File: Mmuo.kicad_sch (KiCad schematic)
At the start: 93 parts, among them IC1 A121-001-T&R, IC2 BQ24253RGER, IC3 ADPL40502AUJZ-1.8-R7, J1 USB_C_Receptacle_USB2.0_16P, J2 B2B-PH-K-S, J3 SW_Debug, Q1 BSS84, Q2 BSS138, Q3 MMBT3904, SW1 PTS815, U1 USBLC6-2SC6, U2 RT9166A-33GXL, U3 EKMB1309113K, U4 STM32WB55CGU6, U5 MCP9808_MSOP, Y1 24MHz, Y2 32MHz, Y3 32K768

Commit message: Schematics Verifcation
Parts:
- added D8: LED, LED_SMD:LED_0805_2012Metric_Pad1.15x1.40mm_HandSolder, symbol Device:LED
- added R24: 220, Resistor_SMD:R_0603_1608Metric_Pad0.98x0.95mm_HandSolder, symbol Device:R
- D1, D2, D3, D6, D7: footprint LED_SMD:LED_1206_3216Metric_Pad1.42x1.75mm_HandSolder -> LED_SMD:LED_0805_2012Metric_Pad1.15x1.40mm_HandSolder
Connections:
- net GND: now also D8.1 (K)
- net Pair_Mode: now reaches U4.29 (PB1)
- net Pair_Mode: now also R24.1
- net RF_LP renamed RF_LPF
- new net: D8.2 (A), R24.2
- no-connect marks 19 -> 18
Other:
- note added: "WHITE"
- note added: "YELLOW"
- note removed: "HSMD-C150"
- note removed: "HSMG-C150"
- moved on the sheet: AE1, AE2, C19, C20, C21, C22, C23, C24, C25, C26, C27, C29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

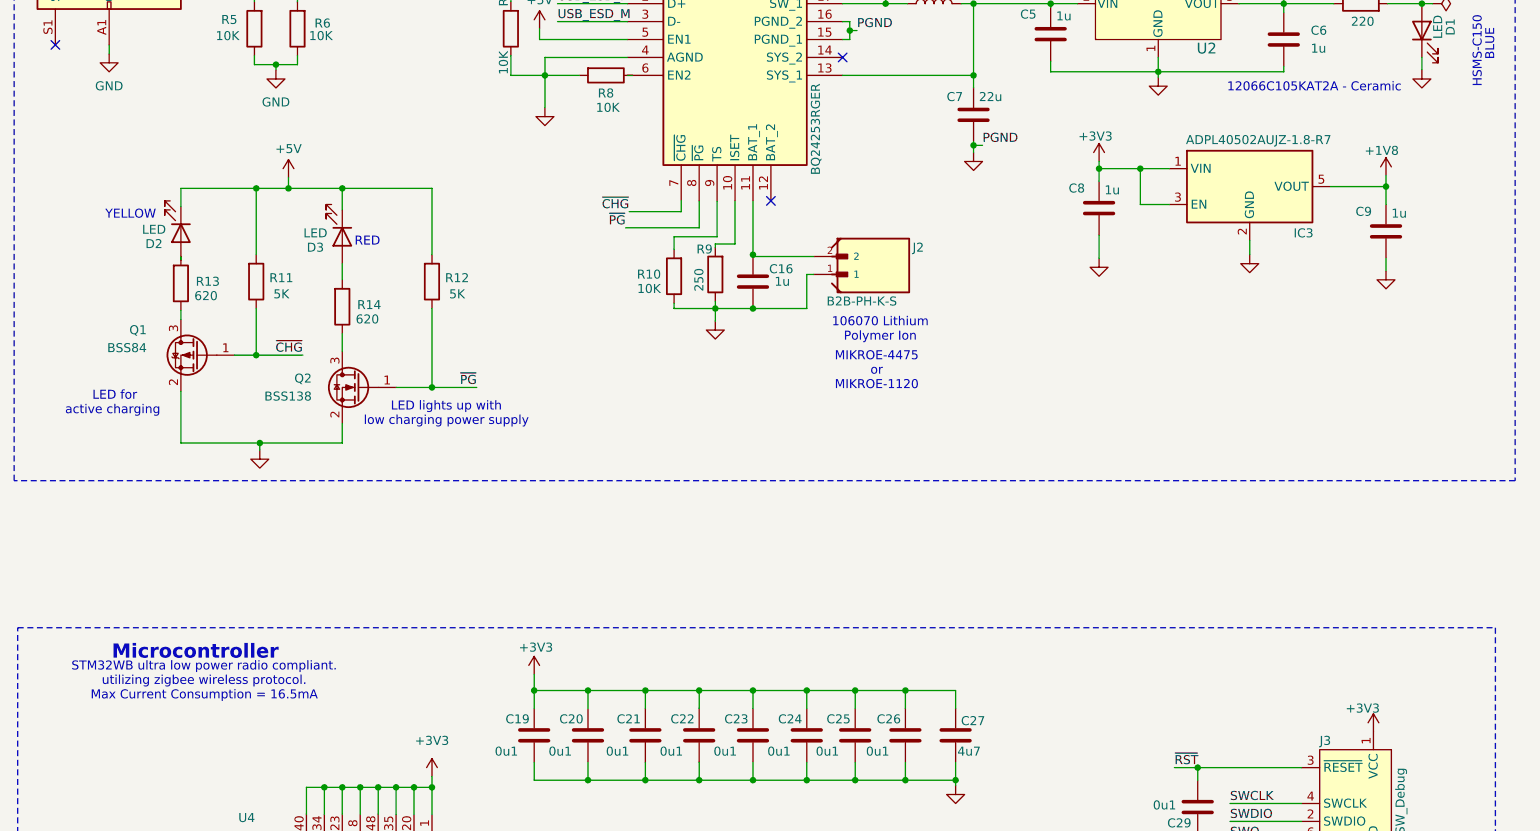
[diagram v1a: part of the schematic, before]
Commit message: replacing 3v3 LDO to boost-buck converter
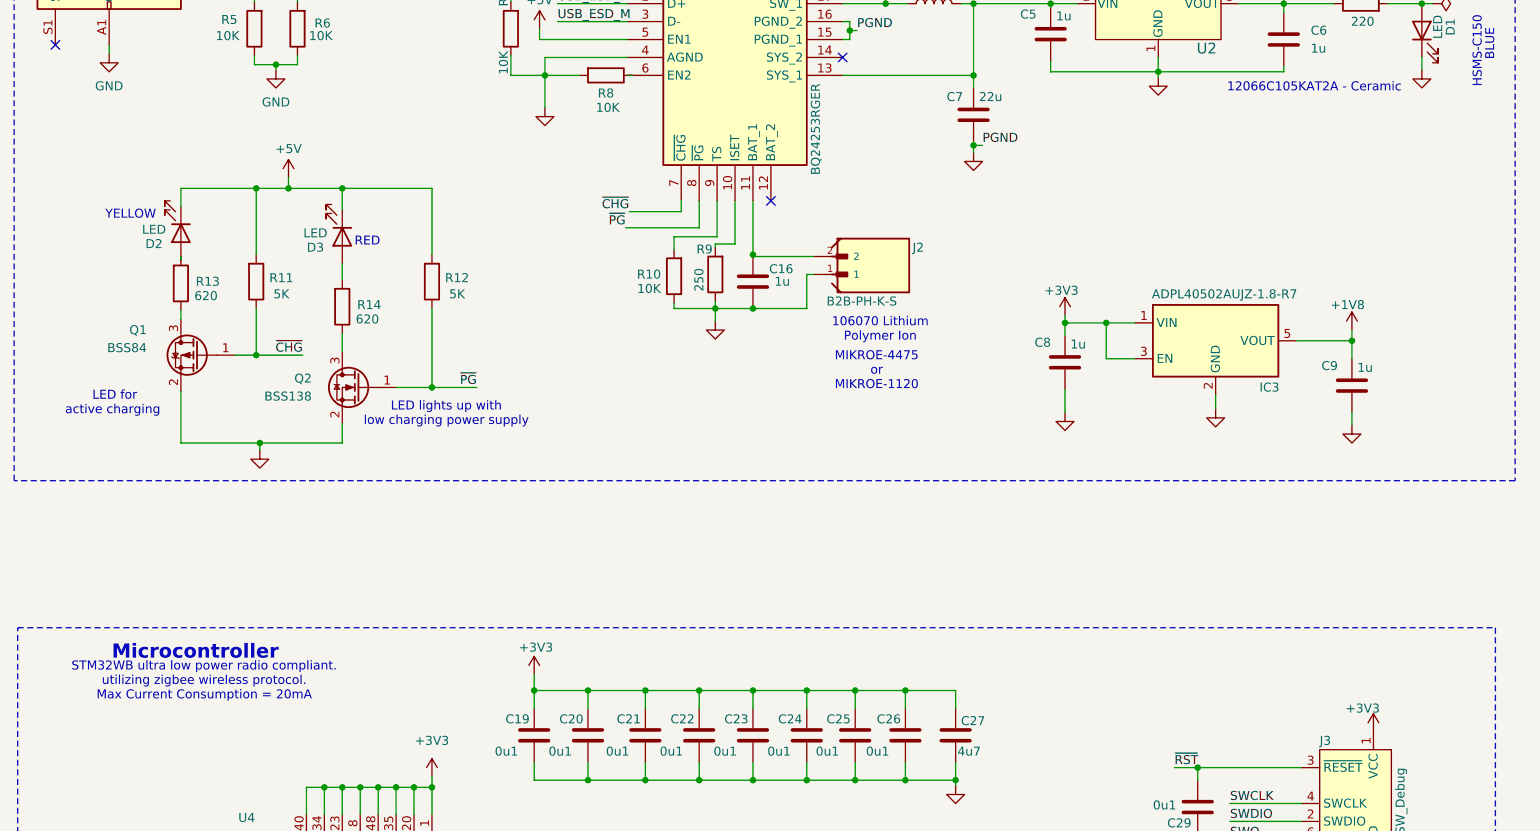
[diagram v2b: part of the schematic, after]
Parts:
- L1: footprint Inductor_SMD:L_0805_2012Metric_Pad1.15x1.40mm_HandSolder -> Inductor_SMD:L_0805_2012Metric_Pad1.05x1.20mm_HandSolder
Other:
- note added: "STM32WB ultra low power radio compliant. utilizing zigbee wireless protocol. Max Current Consumption = 20mA"
- note removed: "STM32WB ultra low power radio compliant. utilizing zigbee wireless protocol. Max Current Consumption = 16.5mA"
- moved on the sheet: C8, C9, IC3

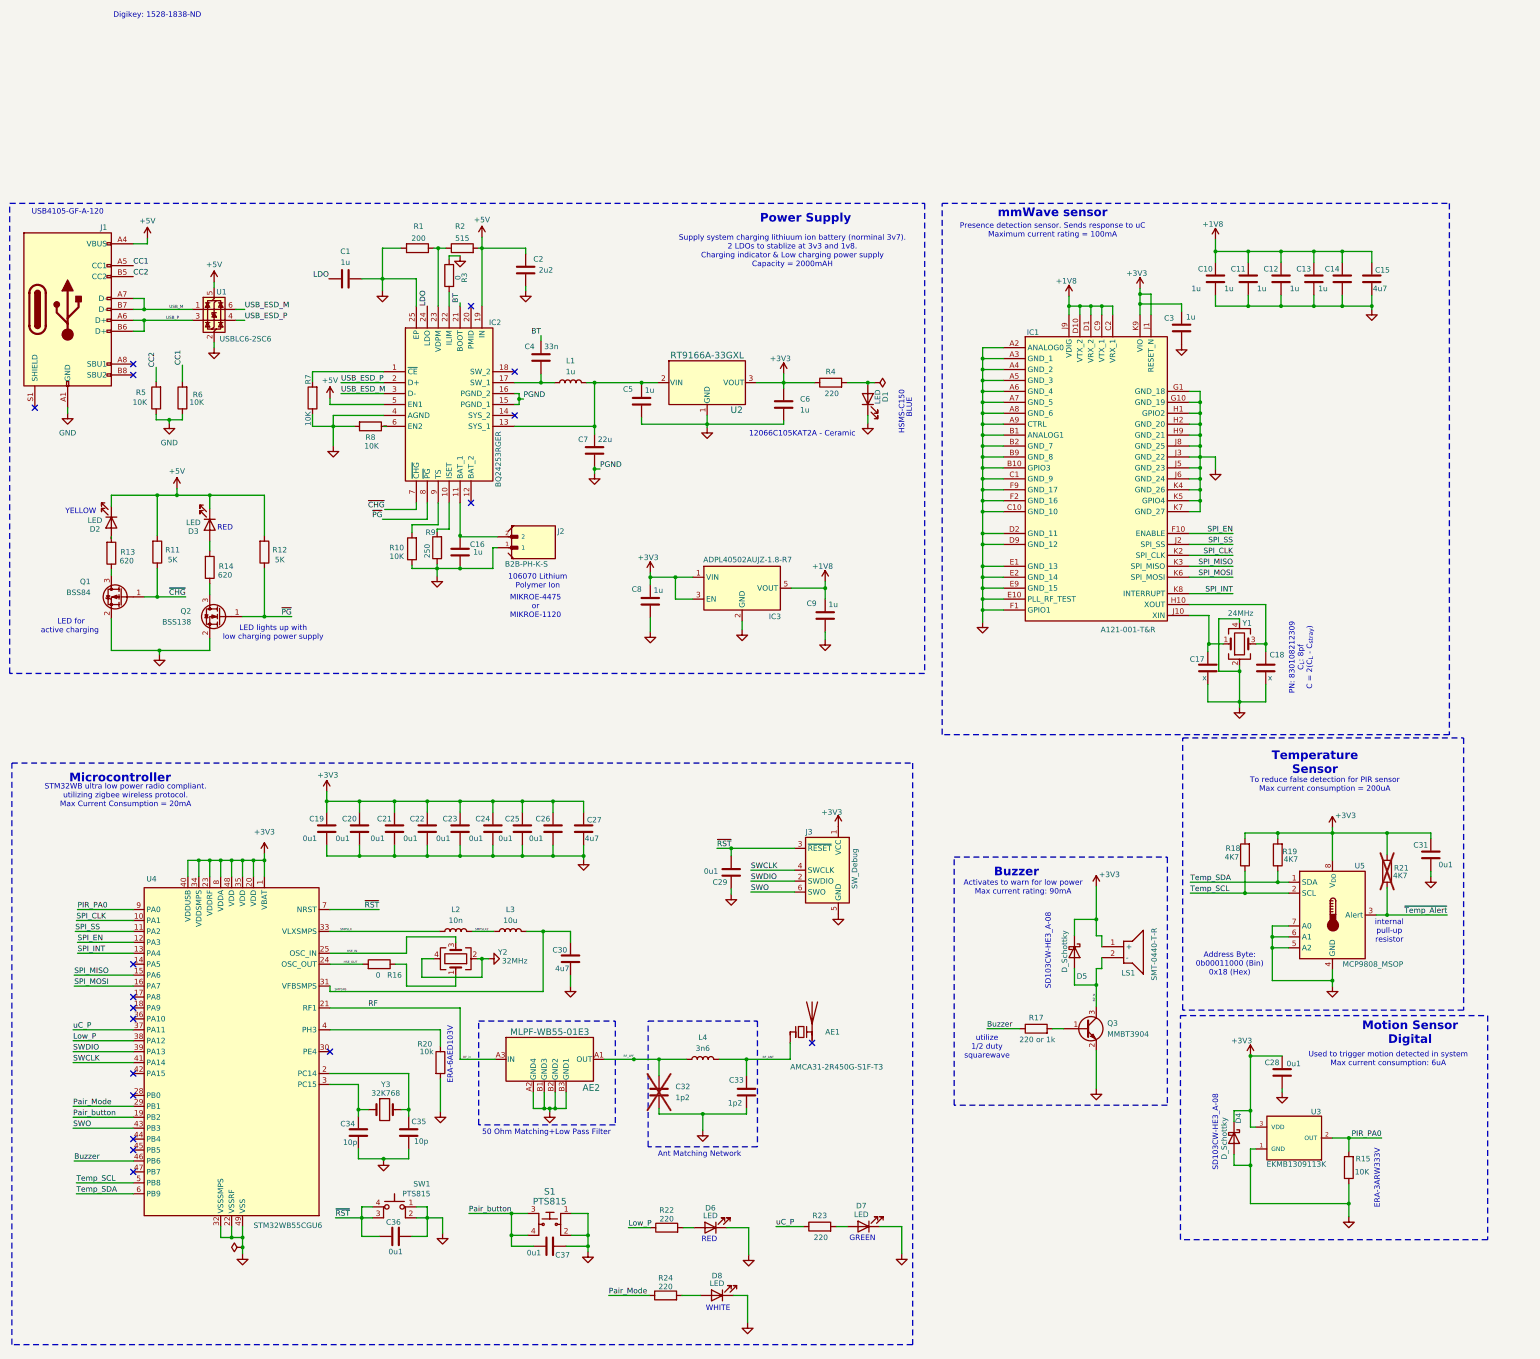
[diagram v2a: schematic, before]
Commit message: replaced LDO and rough cut of pcb
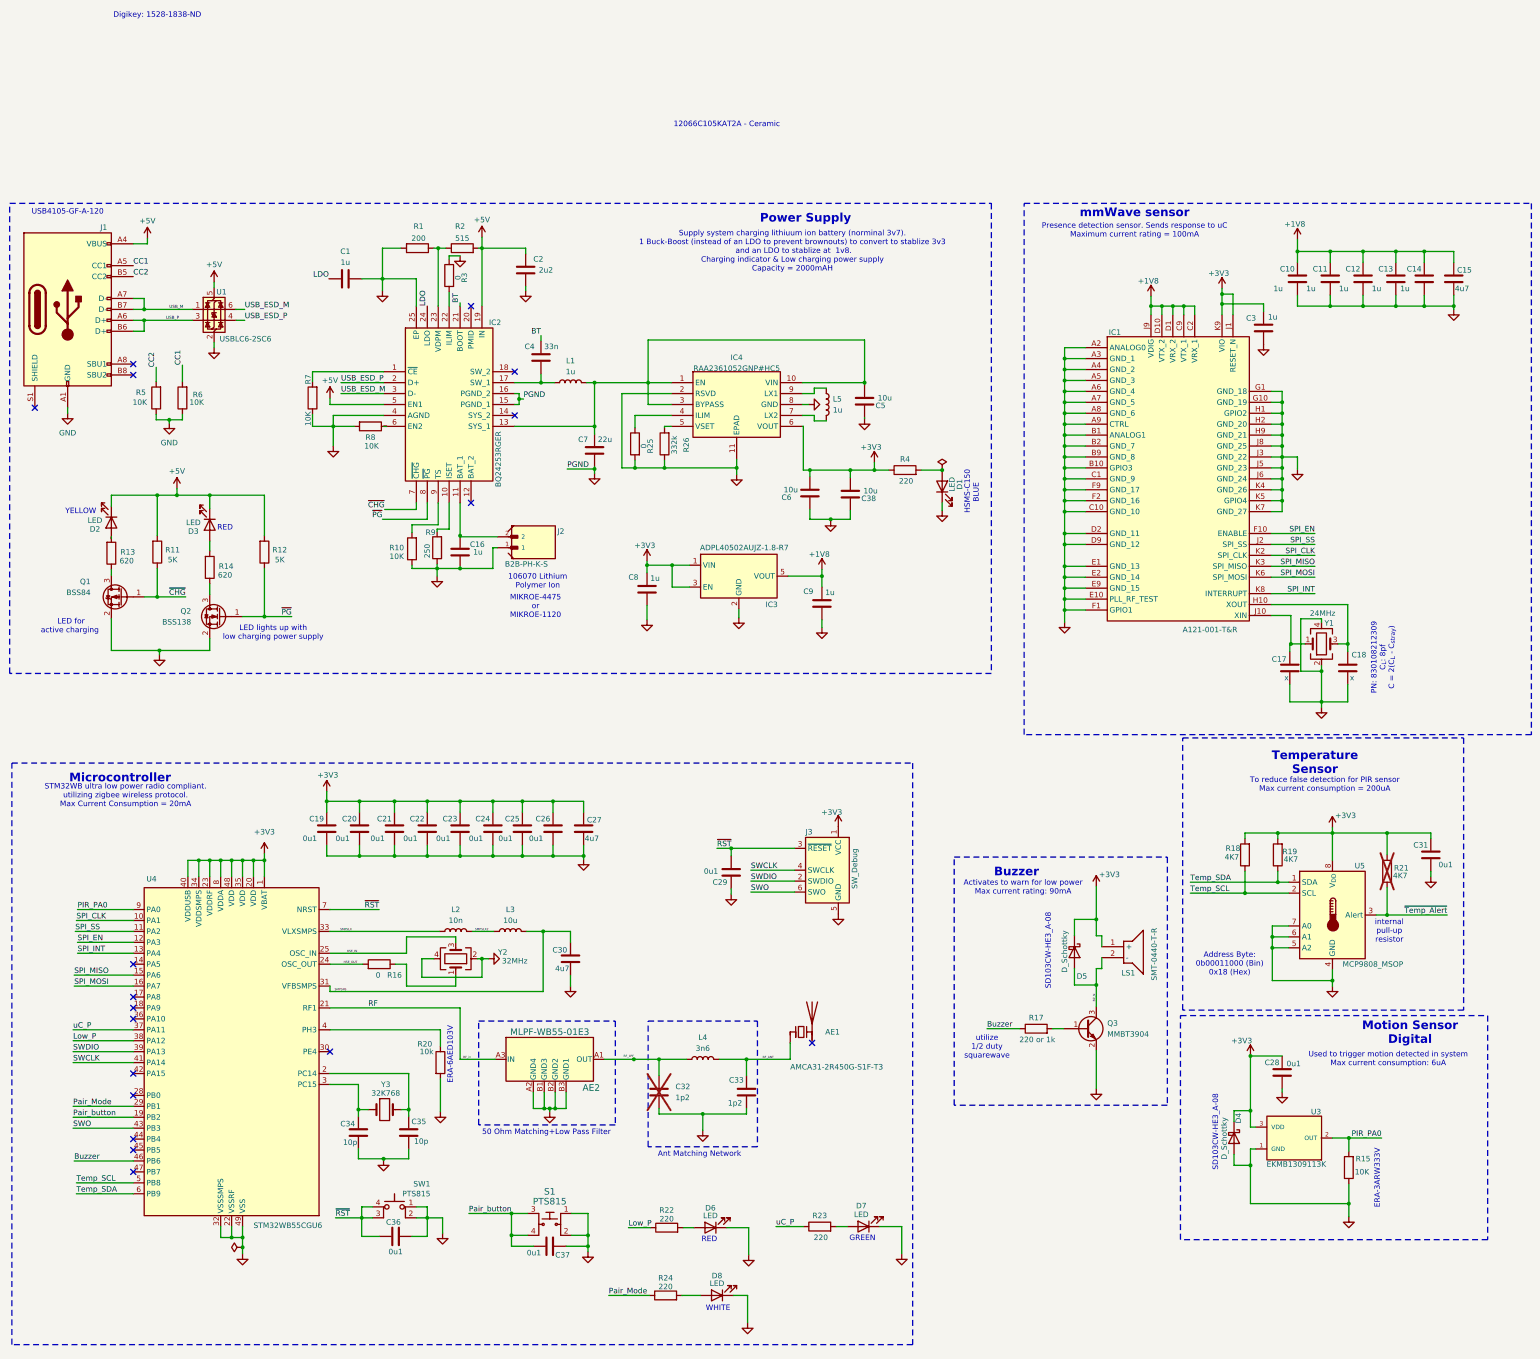
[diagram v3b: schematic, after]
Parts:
- removed U2: RT9166A-33GXL, RT9166A_33GXL:VREG_AP7370-33Y-13, symbol RT9166A_33GXL:RT9166A-33GXL
- added C38: 10u, Capacitor_SMD:C_0603_1608Metric_Pad1.08x0.95mm_HandSolder, symbol Device:C
- added IC4: RAA2361052GNP#HC5, RAA2361052GNP:SON50P250X250X90-11N-D, symbol RAA2361052GNP#HC5:RAA2361052GNP#HC5
- added L5: 1u, Inductor_SMD:L_0805_2012Metric_Pad1.05x1.20mm_HandSolder, symbol Device:L
- added R25: 0, Resistor_SMD:R_0603_1608Metric_Pad0.98x0.95mm_HandSolder, symbol Device:R
- added R26: 332k, Resistor_SMD:R_0603_1608Metric_Pad0.98x0.95mm_HandSolder, symbol Device:R
- C5, C6: value 1u -> 10u
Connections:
- net +3V3: now also C38.1, IC4.6 (VOUT)
- net GND: now also C38.2, IC4.11 (EPAD), IC4.2 (RSVD), IC4.8 (GND), R25.2, R26.1
- net at C5.1, C7.1, IC2.13 (SYS_1)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: now also IC4.1 (EN), IC4.10 (VIN), IC4.3 (BYPASS)
- new net: IC4.5 (VSET), R26.2
- new net: IC4.9 (LX1), L5.1
- new net: IC4.7 (LX2), L5.2
- new net: IC4.4 (ILIM), R25.1
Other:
- note added: "Supply system charging lithiuum ion battery (norminal 3v7). 1 Buck-Boost (instead of an LDO to prevent brownouts) to convert to stablize 3v3 and an LDO to stablize at 1v8. Charging indicator & Low charging power supply Capacity = 2000mAH"
- note removed: "Supply system charging lithiuum ion battery (norminal 3v7). 2 LDOs to stablize at 3v3 and 1v8. Charging indicator & Low charging power supply Capacity = 2000mAH"
- moved on the sheet: C10, C11, C12, C13, C14, C15, C17, C18, C3, C8, C9, D1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

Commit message: Layout and initial routing
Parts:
- added H1, H2, H3, H4: MountingHole_Pad, MountingHole:MountingHole_3.2mm_M3_DIN965_Pad_TopBottom, symbol Mechanical:MountingHole_Pad
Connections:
- net GND: now also H1.1, H2.1, H3.1, H4.1
- net USB_ESD_M renamed USB_ESD_N
- net USB_M renamed USB_N
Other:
- note added: "~{CHG} is pulled low when a charge cycle starts and remains low while charging"
- note added: "~{PG} is pulled low when a valid supply is connected to IN"

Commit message: PCB design and full verification
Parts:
- C31, R18, R19, U5: now not fitted; now left out of the parts list
- R21: now left out of the parts list
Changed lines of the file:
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@@
 		(unit 1)
 		(exclude_from_sim no)
-		(in_bom yes)
-		(on_board yes)
-		(dnp no)
+		(in_bom no)
+		(on_board no)
+		(dnp yes)
 		(property "Reference" "R19"
 			(at 310.388 163.068 0)
@@
 		(unit 1)
 		(exclude_from_sim no)
-		(in_bom yes)
-		(on_board yes)
-		(dnp no)
+		(in_bom no)
+		(on_board no)
+		(dnp yes)
 		(fields_autoplaced yes)
 		(property "Reference" "#PWR051"
@@
 			)
 		)
+		(property "Untitled Field" ""
+			(at 320.294 194.31 0)
+			(effects
+				(font
+					(size 1.27 1.27)
+				)
+				(hide yes)
+			)
+		)
 		(pin "1"
 		)
@@
 		(unit 1)
 		(exclude_from_sim no)
-		(in_bom yes)
-		(on_board yes)
+		(in_bom no)
+		(on_board no)
 		(dnp yes)
 		(property "Reference" "R21"
@@
 		(unit 1)
 		(exclude_from_sim no)
-		(in_bom yes)
-		(on_board yes)
-		(dnp no)
+		(in_bom no)
+		(on_board no)
+		(dnp yes)
 		(property "Reference" "R18"
 			(at 297.18 162.306 0)
@@
 			)
 		)
+		(property "Untitled Field" ""
+			(at 299.974 163.83 0)
+			(effects
+				(font
+					(size 1.27 1.27)
+				)
+				(hide yes)
+			)
+		)
 		(pin "2"
 		)
@@
 		(unit 1)
 		(exclude_from_sim no)
-		(in_bom yes)
-		(on_board yes)
-		(dnp no)
+		(in_bom no)
+		(on_board no)
+		(dnp yes)
 		(property "Reference" "#PWR044"
 			(at 320.294 161.29 0)
@@
 			)
 		)
+		(property "Untitled Field" ""
+			(at 320.294 157.48 0)
+			(effects
+				(font
+					(size 1.27 1.27)
+				)
+				(hide yes)
+			)
+		)
 		(pin "1"
 		)
@@
 		(unit 1)
 		(exclude_from_sim no)
-		(in_bom yes)
-		(on_board yes)
-		(dnp no)
+		(in_bom no)
+		(on_board no)
+		(dnp yes)
 		(property "Reference" "C31"
 			(at 339.09 161.544 0)
@@
 			)
 		)
+		(property "Untitled Field" ""
+			(at 343.154 163.83 0)
+			(effects
+				(font
+					(size 1.27 1.27)
+				)
+				(hide yes)
+			)
+		)
 		(pin "1"
 		)
@@
 		(unit 1)
 		(exclude_from_sim no)
-		(in_bom yes)
-		(on_board yes)
-		(dnp no)
+		(in_bom no)
+		(on_board no)
+		(dnp yes)
 		(property "Reference" "U5"
 			(at 326.644 166.37 0)
